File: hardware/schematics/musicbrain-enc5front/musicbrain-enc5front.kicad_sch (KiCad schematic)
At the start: 8 parts, among them J1 NAAR RISER (achterzijde), SW1 EC11E (switch), SW2 EC11E (switch), SW3 EC11E (switch), SW4 EC11E (switch), SW5 EC11E (switch), U1 MCP23017-E/ML

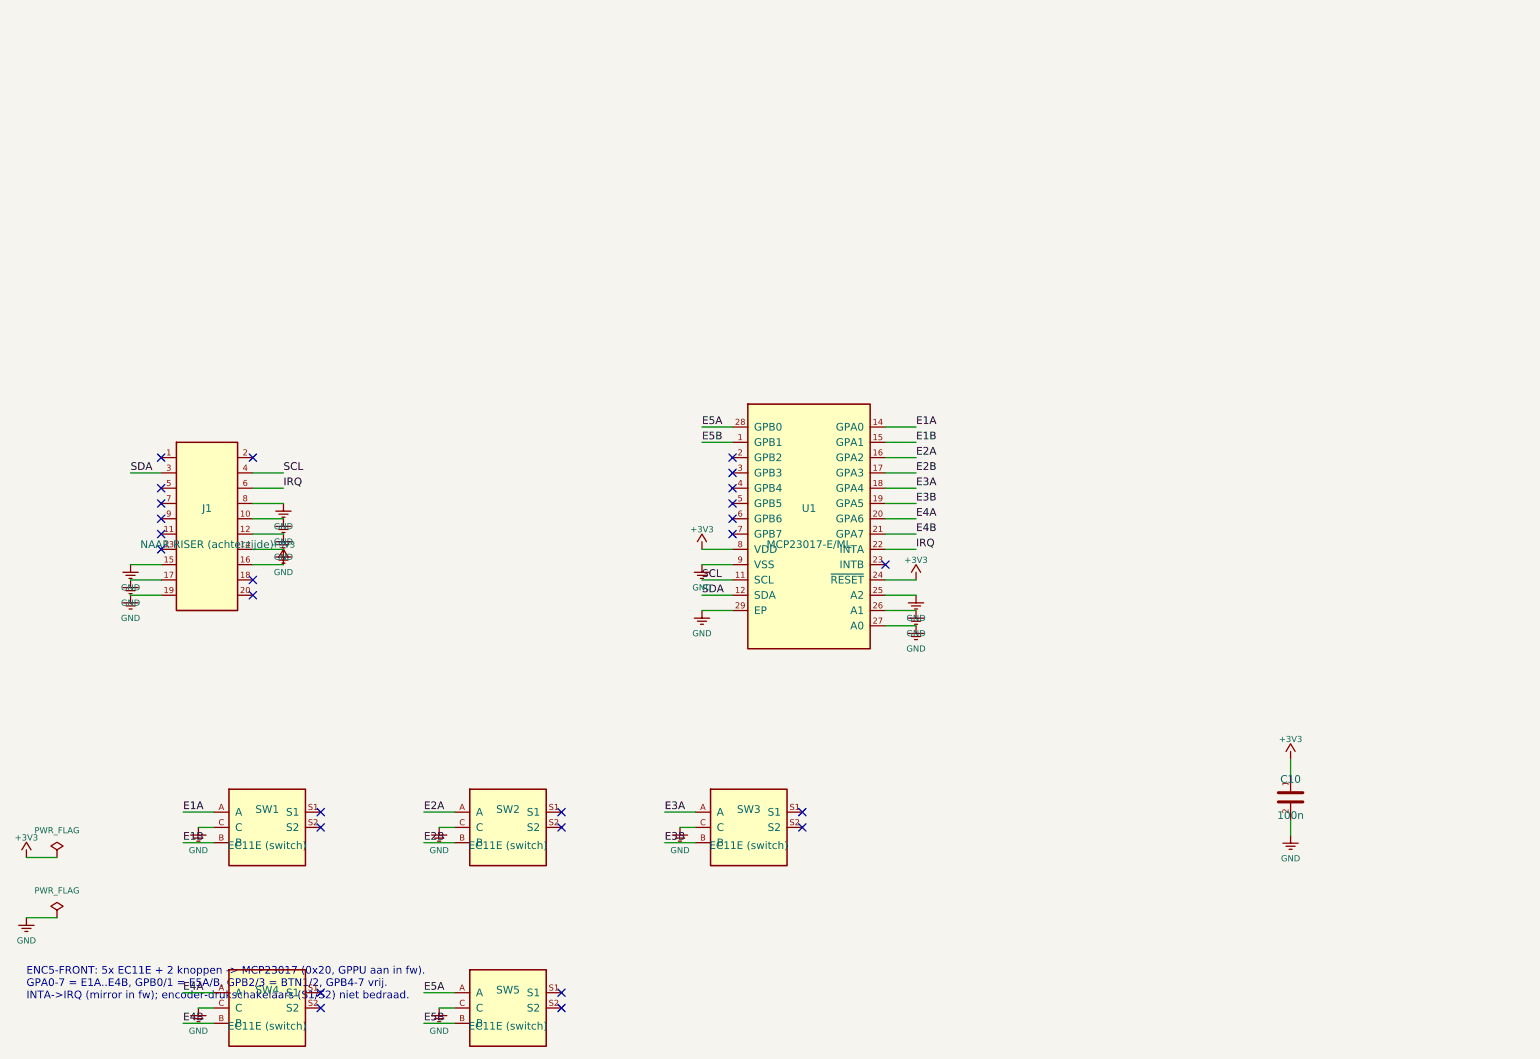
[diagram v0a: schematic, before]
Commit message: ENC5-FRONT rev 2.0 + i2criser: herontwerp op de front-koppel-standaard
ENC5-FRONT 2.0 (30x110, DRC 0/0 + fab):
- 1x10-socket op de front-koppel-standaard (x=116,5 / pin1 y=143,57) i.p.v.
  de 2x10-riser-socket middenop (paste mechanisch niet - besluit Mark)
- encoders 90 graden gedraaid (socketkolom vrij), steek 17,6, hartlijn 8,0;
  bord 30 mm breed (front zit uiterst links/rechts in het paneel)
- 2x MCP23017 (0x20/0x21) = 32 bits: drukassen bedraad, 2 knopjes terug,
  2x8-expansieheader voor display-deel (2 encoders + 4 knoppen + 2 spares)
- routing: freerouting-pijplijn (beste-van-N-lus), clearance 0,15-netclass,
  X_E7S handroute; netcheck + DRC 0/0

Nieuw bord musicbrain-i2criser rev 1.0 (DRC 0/0 + fab): domme I2C-doorlus
slot -> 1x10-front (potriser-mechanica, geen componenten).

Toolkit: cardlib paper-instelling + PNET-registratie + snap_stubs();
seslib apply_ses(only=/skip=); make_fab bordenlijst + i2criser.
README's: enc5front herschreven, i2criser nieuw, jack8/jack4/pot8front/
riser bijgewerkt (versies + standaard + riser-familie).

Co-Authored-By: Claude Fable 5 <noreply@anthropic.com>
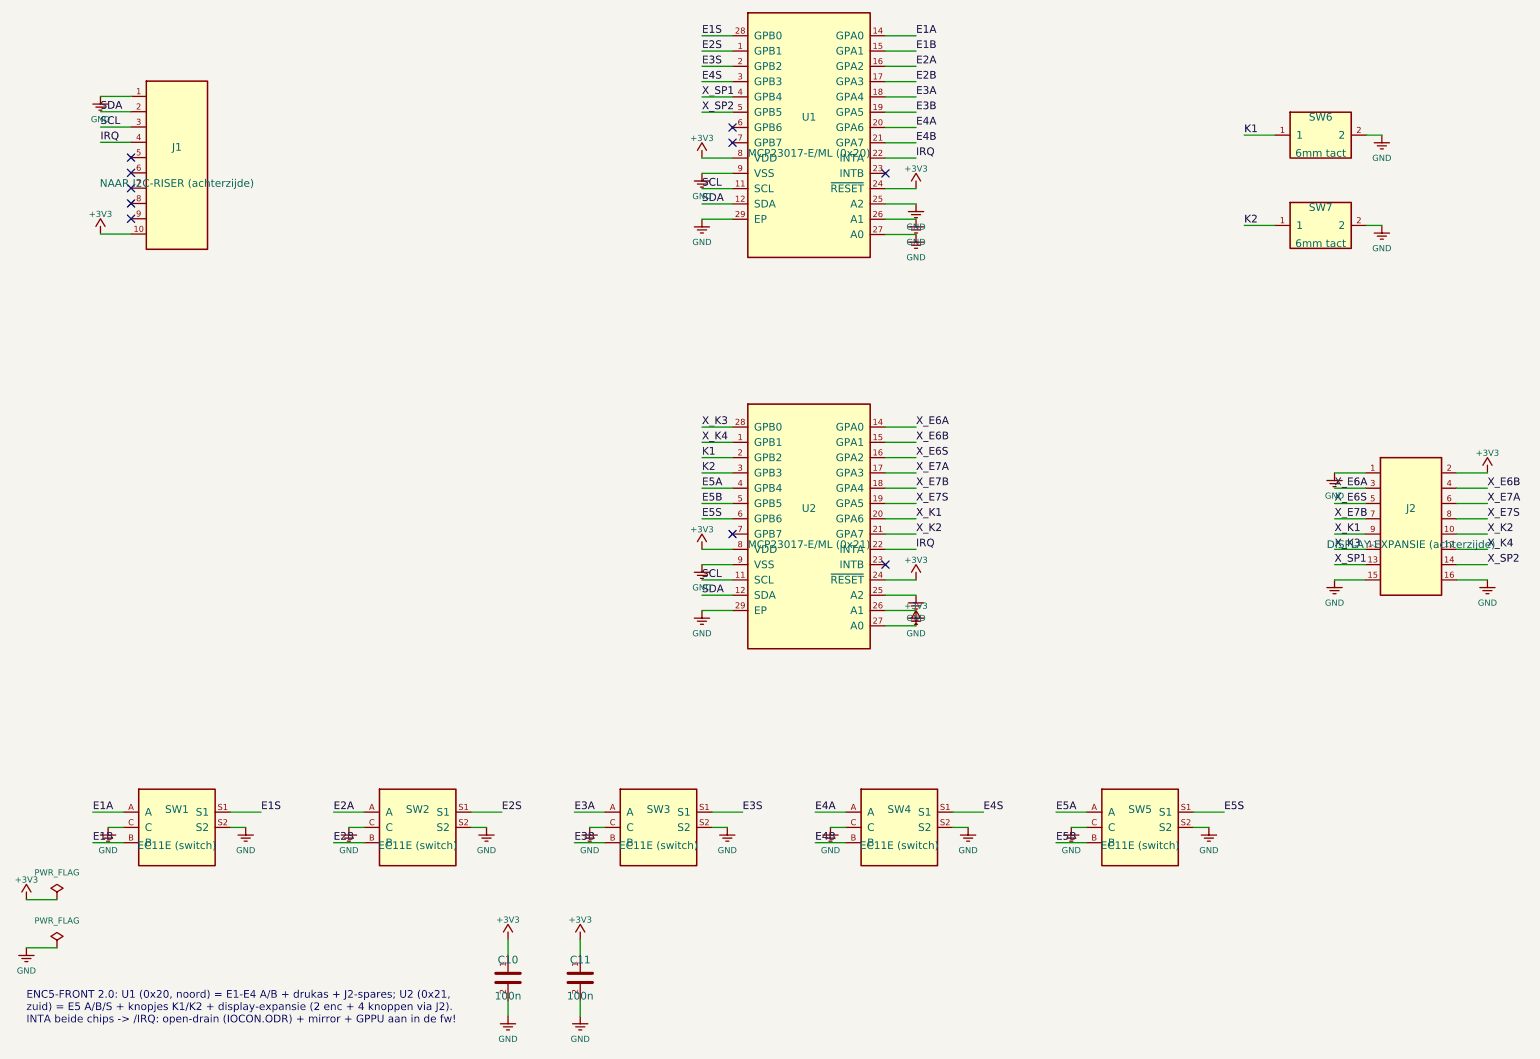
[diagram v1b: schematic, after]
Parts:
- added C11: 100n, Capacitor_SMD:C_0805_2012Metric, symbol Device:C
- added J2: DISPLAY-EXPANSIE (achterzijde), MusicBrain:Header_2x08_backside, symbol Custom:Conn_02x08
- added SW6, SW7: 6mm tact, Button_Switch_THT:SW_PUSH_6mm, symbol Custom:SW_PUSH
- added U2: MCP23017-E/ML (0x21), Package_DFN_QFN:QFN-28-1EP_6x6mm_P0.65mm_EP4.25x4.25mm, symbol Custom:MCP23017Q
- J1: value NAAR RISER (achterzijde) -> NAAR I2C-RISER (achterzijde); footprint MusicBrain:Socket_2x10_backside -> MusicBrain:Socket_1x10_backside; symbol Custom:Conn_02x10 -> Custom:Conn_01x10
- U1: value MCP23017-E/ML -> MCP23017-E/ML (0x20)
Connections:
- net +3V3: now also J1.10 (Pin_10), C11.1, J2.2 (Pin_2), U2.24 (~{RESET}), U2.27 (A0), U2.8 (VDD); no longer J1.16 (Pin_16)
- net E5A: now also U2.4 (GPB4); no longer U1.28 (GPB0)
- net E5B: now also U2.5 (GPB5); no longer U1.1 (GPB1)
- net GND: now also J1.1 (Pin_1), SW1.S2, SW2.S2, SW3.S2, SW4.S2, SW5.S2, C11.2, J2.1 (Pin_1), J2.15 (Pin_15), J2.16 (Pin_16), SW6.2, SW7.2, U2.25 (A2), U2.26 (A1), U2.29 (EP), U2.9 (VSS); no longer J1.10 (Pin_10), J1.12 (Pin_12), J1.14 (Pin_14), J1.15 (Pin_15), J1.17 (Pin_17), J1.19 (Pin_19), J1.8 (Pin_8)
- net IRQ: now also J1.4 (Pin_4), U2.22 (INTA); no longer J1.6 (Pin_6)
- net SCL: now also J1.3 (Pin_3), U2.11 (SCL); no longer J1.4 (Pin_4)
- net SDA: now also J1.2 (Pin_2), U2.12 (SDA); no longer J1.3 (Pin_3)
- net E3S: now reaches U1.2 (GPB2)
- net E3S: now also SW3.S1
- net E4S: now reaches U1.3 (GPB3)
- net E4S: now also SW4.S1
- net X_SP1: now reaches U1.4 (GPB4)
- net X_SP1: now also J2.13 (Pin_13)
- net X_SP2: now reaches U1.5 (GPB5)
- net X_SP2: now also J2.14 (Pin_14)
- net E1S: now reaches SW1.S1
- net E1S: now also U1.28 (GPB0)
- net E2S: now reaches SW2.S1
- net E2S: now also U1.1 (GPB1)
- net E5S: now reaches SW5.S1
- net E5S: now also U2.6 (GPB6)
- new net K1: SW6.1, U2.2 (GPB2)
- new net K2: SW7.1, U2.3 (GPB3)
- new net X_E6A: J2.3 (Pin_3), U2.14 (GPA0)
- new net X_E6B: J2.4 (Pin_4), U2.15 (GPA1)
- new net X_E6S: J2.5 (Pin_5), U2.16 (GPA2)
- new net X_E7A: J2.6 (Pin_6), U2.17 (GPA3)
- new net X_E7B: J2.7 (Pin_7), U2.18 (GPA4)
- new net X_E7S: J2.8 (Pin_8), U2.19 (GPA5)
- new net X_K1: J2.9 (Pin_9), U2.20 (GPA6)
- new net X_K2: J2.10 (Pin_10), U2.21 (GPA7)
- new net X_K3: J2.11 (Pin_11), U2.28 (GPB0)
- new net X_K4: J2.12 (Pin_12), U2.1 (GPB1)
- no-connect marks 26 -> 10
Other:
- note added: "ENC5-FRONT 2.0: U1 (0x20, noord) = E1-E4 A/B + drukas + J2-spares; U2 (0x21, zuid) = E5 A/B/S + knopjes K1/K2 + display-expansie (2 enc + 4 knoppen via J2). INTA beide chips -> /IRQ: open-drain (IOCON.ODR) + mirror + GPPU aan in de fw!"
- note removed: "ENC5-FRONT: 5x EC11E + 2 knoppen -> MCP23017 (0x20, GPPU aan in fw). GPA0-7 = E1A..E4B, GPB0/1 = E5A/B, GPB2/3 = BTN1/2, GPB4-7 vrij. INTA->IRQ (mirror in fw); encoder-drukschakelaars (S1/S2) niet bedraad."
- title: MusicBrain ENC5-FRONT - 5x encoder op de generieke riser -> MusicBrain ENC5-FRONT - 5x encoder + 2 knoppen + display-expansie
